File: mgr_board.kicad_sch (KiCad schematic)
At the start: 48 parts, among them IC1 MCP48CVB08-20E_ST, J1 Screw_Terminal_2_P5.00mm

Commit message: wip
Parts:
- added R49, R50, R51, R52, R53, R54, R55, R56, R57, R58, R59, R60, R61, R62: NMT, Resistor_SMD:R_0402_1005Metric, symbol PCM_SL_Resistors:Resistor
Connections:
- net +3V3: now also R1.2; no longer TH1.1
- net ADC0_CS: now also R55.2; no longer A1.2 (GP1)
- net ADC1_CS: now also R54.2; no longer A1.7 (GP5)
- net ADC2_CS: now also R57.2; no longer A1.12 (GP9)
- net ADC_NTC: now also R1.1, TH1.1; no longer R1.2, TH1.2
- net ADIM_2: now also IC1.13 (VOUT5); no longer IC1.7 (VOUT4)
- net ADIM_3: now also IC1.7 (VOUT4); no longer IC1.13 (VOUT5)
- net ADIM_4: now also IC1.14 (VOUT3); no longer IC1.6 (VOUT2)
- net ADIM_5: now also IC1.6 (VOUT2); no longer IC1.14 (VOUT3)
- net DAC_CS: now also R51.2; no longer A1.17 (GP13)
- net GND: now also TH1.2; no longer R1.1
- net SD_CS: now also R56.1; no longer A1.22 (GP17)
- net SPI0_MISO: now also R58.1, R59.1, R60.1; no longer ADC1.26 (DOUT/~{DRDY}), ADC2.26 (DOUT/~{DRDY}), ADC3.26 (DOUT/~{DRDY})
- net SPI0_MOSI: now also R52.2; no longer A1.5 (GP3)
- net SPI0_SCL: now also R53.2; no longer A1.4 (GP2)
- net SPI1_MISO: now also R61.1, R62.1; no longer IC1.17 (SDO)
- net SPI1_MOSI: now also R49.2; no longer A1.15 (GP11)
- net SPI1_SCL: now also R50.2; no longer A1.14 (GP10)
- new net: A1.5 (GP3), R52.1
- new net: ADC3.26 (DOUT/~{DRDY}), R58.2
- new net: A1.12 (GP9), R57.1
- new net: A1.14 (GP10), R50.1
- new net: A1.15 (GP11), R49.1
- new net: A1.17 (GP13), R51.1
- new net: A1.2 (GP1), R55.1
- new net: A1.22 (GP17), R56.2
- new net: A1.4 (GP2), R53.1
- new net: A1.7 (GP5), R54.1
- new net: ADC1.26 (DOUT/~{DRDY}), R60.2
- new net: ADC2.26 (DOUT/~{DRDY}), R59.2
- new net: IC1.17 (SDO), R61.2
- new net Micro_SD/SPI1_MISO: R62.2
- no-connect marks 26 -> 27
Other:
- moved on the sheet: R1, TH1

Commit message: wip
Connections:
- net +12V: now also J1.1; no longer J1.2
- net GND: now also J1.2; no longer J1.1
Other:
- moved on the sheet: J1
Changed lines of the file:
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@@
 	)
 	(junction
-		(at 201.93 26.67)
+		(at 27.94 153.67)
 		(diameter 0)
 		(color 0 0 0 0)
 	)
 	(junction
-		(at 27.94 153.67)
+		(at 201.93 26.67)
 		(diameter 0)
 		(color 0 0 0 0)
@@
 	(wire
 		(pts
+			(xy 24.13 156.21) (xy 27.94 156.21)
+		)
+		(stroke
+			(width 0)
+			(type default)
+		)
+	)
+	(wire
+		(pts
 			(xy 271.78 110.49) (xy 260.35 110.49)
 		)
@@
 	(wire
 		(pts
-			(xy 25.4 153.67) (xy 27.94 153.67)
-		)
-		(stroke
-			(width 0)
-			(type default)
-		)
-	)
-	(wire
-		(pts
 			(xy 125.73 92.71) (xy 134.62 92.71)
 		)
@@
 	(wire
 		(pts
-			(xy 27.94 156.21) (xy 25.4 156.21)
-		)
-		(stroke
-			(width 0)
-			(type default)
-		)
-	)
-	(wire
-		(pts
 			(xy 260.35 41.91) (xy 261.62 41.91)
 		)
@@
 	(wire
 		(pts
+			(xy 24.13 153.67) (xy 27.94 153.67)
+		)
+		(stroke
+			(width 0)
+			(type default)
+		)
+	)
+	(wire
+		(pts
 			(xy 260.35 31.75) (xy 280.67 31.75)
 		)
@@
 	(symbol
 		(lib_id "PCM_SL_Screw_Terminal:Screw_Terminal_2_P5.00mm")
-		(at 21.59 154.94 180)
+		(at 20.32 154.94 0)
+		(mirror y)
 		(unit 1)
 		(exclude_from_sim no)
@@
 		(dnp no)
 		(property "Reference" "J1"
-			(at 17.78 156.2101 0)
+			(at 16.51 153.6699 0)
 			(effects
 				(font
@@
 		)
 		(property "Value" "Screw_Terminal_2_P5.00mm"
-			(at 38.608 147.32 0)
+			(at 37.338 162.56 0)
 			(effects
 				(font
@@
 		)
 		(property "Footprint" "TerminalBlock:TerminalBlock_bornier-2_P5.08mm"
-			(at 20.32 148.59 0)
+			(at 19.05 161.29 0)
 			(effects
 				(font
@@
 		)
 		(property "Datasheet" ""
-			(at 21.59 154.94 0)
+			(at 20.32 154.94 0)
 			(effects
 				(font
@@
 		)
 		(property "Description" ""
-			(at 21.59 154.94 0)
+			(at 20.32 154.94 0)
 			(effects
 				(font

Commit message: finished boarD
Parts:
- C1, C3: LCSC (none) -> C19666
- C10, C11, C12, C13, C2, C4, C8, C9: LCSC (none) -> C14663
- C5, C6, C7: LCSC (none) -> C15849
- R1: LCSC (none) -> C21190
- R2, R3, R4: LCSC (none) -> C25804

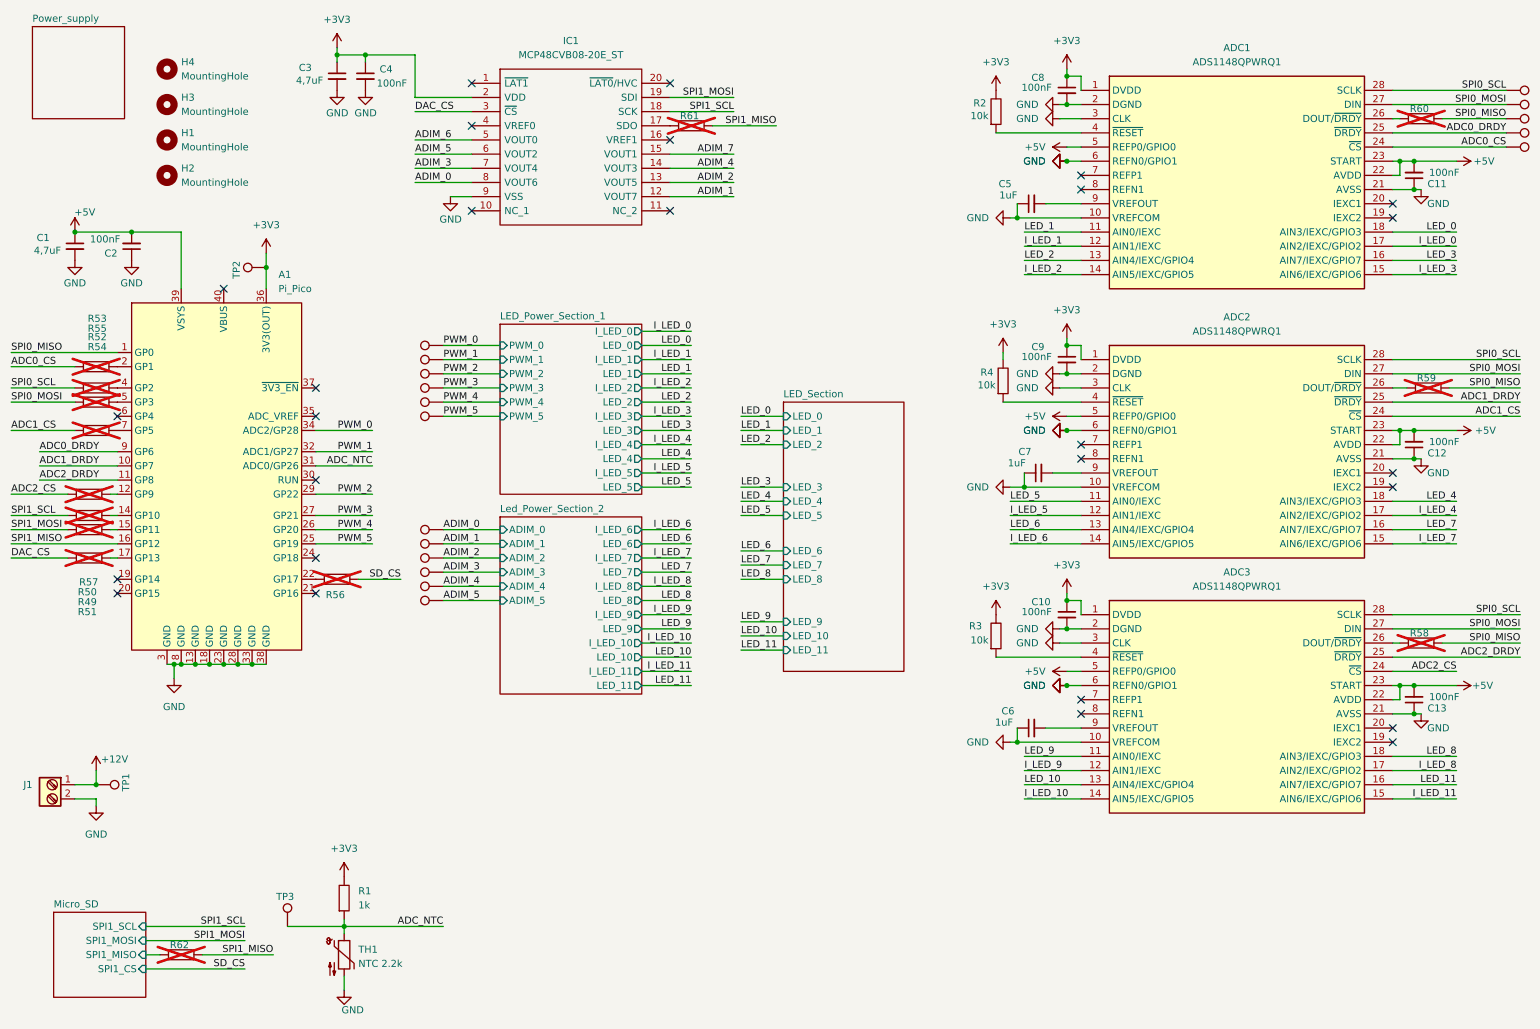
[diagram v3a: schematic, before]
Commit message: Added current sense amplifier, reduced one ADC, changed elec cap to tantals, to review
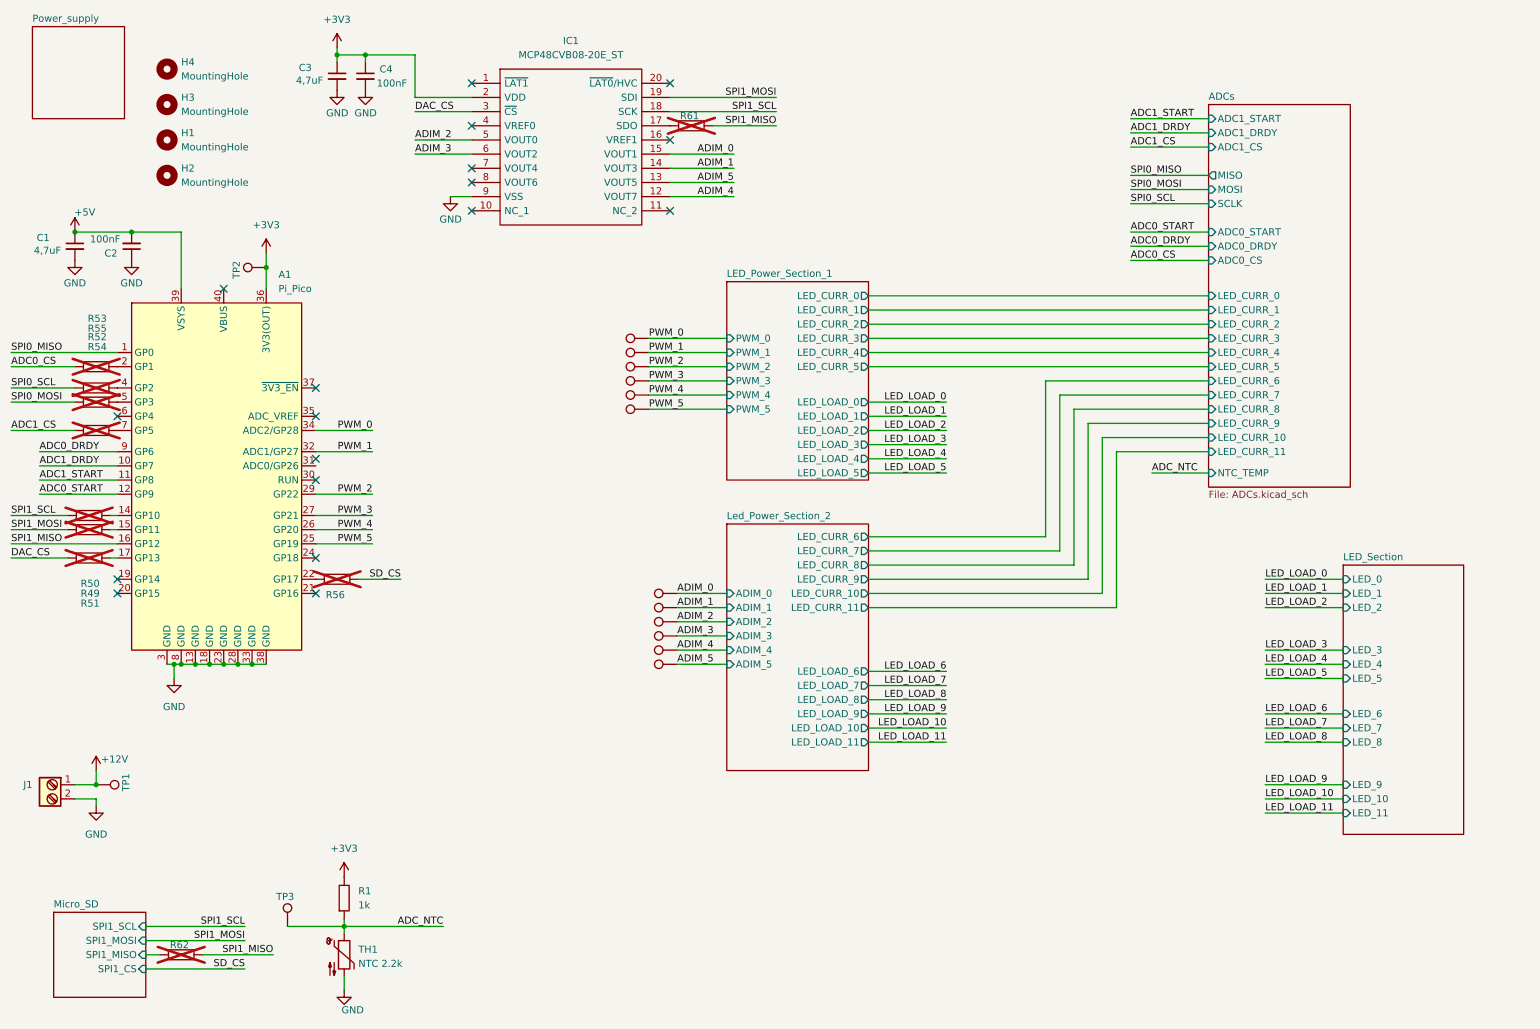
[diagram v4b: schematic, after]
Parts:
- removed ADC1, ADC2, ADC3: ADS1148QPWRQ1, Package_SO:TSSOP-28_4.4x9.7mm_P0.65mm, symbol ADS1148QPWRQ1:ADS1148QPWRQ1
- removed C10, C11, C12, C13, C8, C9: 100nF, Capacitor_SMD:C_0603_1608Metric_Pad1.08x0.95mm_HandSolder, symbol Device:C_Small
- removed C5, C6, C7: 1uF, Capacitor_SMD:C_0603_1608Metric_Pad1.08x0.95mm_HandSolder, symbol Device:C_Small
- removed R2, R3, R4: 10k, Resistor_SMD:R_0603_1608Metric_Pad0.98x0.95mm_HandSolder, symbol PCM_SL_Resistors:Resistor
- removed R57, R58, R59, R60: NMT, Resistor_SMD:R_0402_1005Metric, symbol PCM_SL_Resistors:Resistor
- removed TP16, TP17, TP18, TP19, TP20: TestPoint, TestPoint:TestPoint_Pad_D2.0mm, symbol Connector:TestPoint
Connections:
- net ADIM_6 is gone; now on net ADIM_2: IC1.5 (VOUT0)
- net ADIM_7 is gone; now on net ADIM_0: IC1.15 (VOUT1)
- net ADC_NTC: no longer A1.31 (ADC0/GP26)
- net ADIM_0: no longer IC1.8 (VOUT6)
- net ADIM_1: now also IC1.14 (VOUT3); no longer IC1.12 (VOUT7)
- net ADIM_2: no longer IC1.13 (VOUT5)
- net ADIM_3: now also IC1.6 (VOUT2); no longer IC1.7 (VOUT4)
- net ADIM_4: now also IC1.12 (VOUT7); no longer IC1.14 (VOUT3)
- net ADIM_5: now also IC1.13 (VOUT5); no longer IC1.6 (VOUT2)
- net ADC0_START: now reaches A1.12 (GP9)
- net ADC2_DRDY renamed ADC1_START
- no-connect marks 27 -> 18
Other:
- added sheet ADCs (ADCs.kicad_sch)
- sheet LED_Power_Section_1 ports: added LED_CURR_0, LED_CURR_1, LED_CURR_2, LED_CURR_3, LED_CURR_4, LED_CURR_5, LED_LOAD_0, LED_LOAD_1, LED_LOAD_2, LED_LOAD_3, LED_LOAD_4, LED_LOAD_5; removed I_LED_0, I_LED_1, I_LED_2, I_LED_3, I_LED_4, I_LED_5, LED_0, LED_1, LED_2, LED_3, LED_4, LED_5
- sheet Led_Power_Section_2 ports: added LED_CURR_10, LED_CURR_11, LED_CURR_6, LED_CURR_7, LED_CURR_8, LED_CURR_9, LED_LOAD_10, LED_LOAD_11, LED_LOAD_6, LED_LOAD_7, LED_LOAD_8, LED_LOAD_9; removed I_LED_10, I_LED_11, I_LED_6, I_LED_7, I_LED_8, I_LED_9, LED_10, LED_11, LED_6, LED_7, LED_8, LED_9

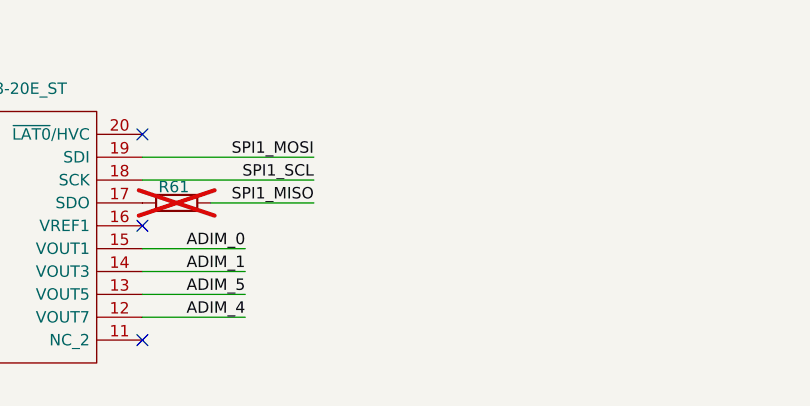
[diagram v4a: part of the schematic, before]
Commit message: Added low pass filters at current sense amp outputs and pull ups on cs pins, DRC done
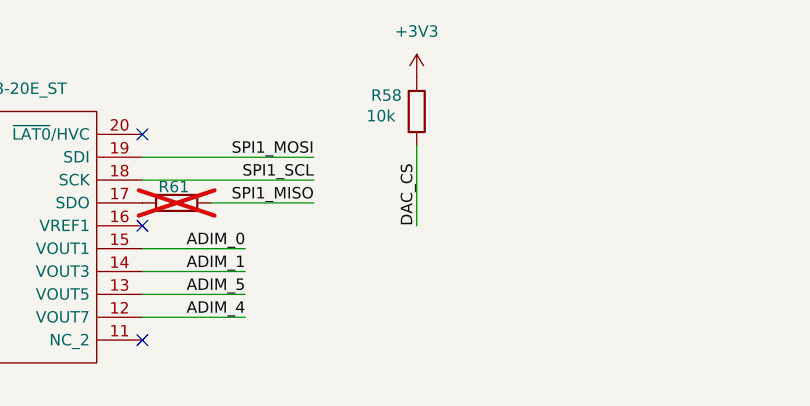
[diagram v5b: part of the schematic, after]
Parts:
- added R58: 10k, Resistor_SMD:R_0603_1608Metric_Pad0.98x0.95mm_HandSolder, symbol PCM_SL_Resistors:Resistor
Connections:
- net +3V3: now also R58.2
- net DAC_CS: now also R58.1
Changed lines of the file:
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@@
+	(wire
+		(pts
+			(xy 161.29 38.1) (xy 161.29 29.21)
+		)
+		(stroke
+			(width 0)
+			(type default)
+		)
+	)
 	(wire
 		(pts
@@
 			)
 			(justify right bottom)
+		)
+	)
+	(label "DAC_CS"
+		(at 161.29 38.1 90)
+		(effects
+			(font
+				(size 1.27 1.27)
+			)
+			(justify left bottom)
 		)
 	)
@@
 	(symbol
 		(lib_id "PCM_SL_Resistors:Resistor")
+		(at 161.29 25.4 90)
+		(unit 1)
+		(exclude_from_sim no)
+		(in_bom yes)
+		(on_board yes)
+		(dnp no)
+		(property "Reference" "R58"
+			(at 156.21 23.622 90)
+			(effects
+				(font
+					(size 1.27 1.27)
+				)
+				(justify right)
+			)
+		)
+		(property "Value" "10k"
+			(at 155.702 25.908 90)
+			(effects
+				(font
+					(size 1.27 1.27)
+				)
+				(justify right)
+			)
+		)
+		(property "Footprint" "Resistor_SMD:R_0603_1608Metric_Pad0.98x0.95mm_HandSolder"
+			(at 165.608 24.511 0)
+			(effects
+				(font
+					(size 1.27 1.27)
+				)
+				(hide yes)
+			)
+		)
+		(property "Datasheet" ""
+			(at 161.29 24.892 0)
+			(effects
+				(font
+					(size 1.27 1.27)
+				)
+				(hide yes)
+			)
+		)
+		(property "Description" "1/4W Resistor"
+			(at 161.29 25.4 0)
+			(effects
+				(font
+					(size 1.27 1.27)
+				)
+				(hide yes)
+			)
+		)
+		(property "LCSC" "C25804"
+			(at 161.29 25.4 0)
+			(effects
+				(font
+					(size 1.27 1.27)
+				)
+				(hide yes)
+			)
+		)
+		(pin "2"
+		)
+		(pin "1"
+		)
+		(instances
+			(project "mgr_board"
+				(path "/14d3b6cb-e4ae-41db-89eb-e86b07bc47b0"
+					(reference "R58")
+					(unit 1)
+				)
+			)
+		)
+	)
+	(symbol
+		(lib_id "PCM_SL_Resistors:Resistor")
 		(at 26.67 107.95 180)
 		(unit 1)
@@
 					(unit 1)
 				)
+			)
+		)
+	)
+	(symbol
+		(lib_id "power:+3V3")
+		(at 161.29 21.59 0)
+		(unit 1)
+		(exclude_from_sim no)
+		(in_bom yes)
+		(on_board yes)
+		(dnp no)
+		(fields_autoplaced yes)
+		(property "Reference" "#PWR0266"
+			(at 161.29 25.4 0)
+			(effects
+				(font
+					(size 1.27 1.27)
+				)
+				(hide yes)
+			)
+		)
+		(property "Value" "+3V3"
+			(at 161.29 16.51 0)
+			(effects
+				(font
+					(size 1.27 1.27)
+				)
+			)
+		)
+		(property "Footprint" ""
+			(at 161.29 21.59 0)
+			(effects
+				(font
+					(size 1.27 1.27)
+				)
+				(hide yes)
+			)
+		)
+		(property "Datasheet" ""
+			(at 161.29 21.59 0)
+			(effects
+				(font
+					(size 1.27 1.27)
+				)
+				(hide yes)
+			)
+		)
+		(property "Description" "Power symbol creates a global label with name \"+3V3\""
+			(at 161.29 21.59 0)
+			(effects
+				(font
+					(size 1.27 1.27)
+				)
+				(hide yes)
+			)
+		)
+		(pin "1"
+		)
+		(instances
+			(project "mgr_board"
+				(path "/14d3b6cb-e4ae-41db-89eb-e86b07bc47b0"
+					(reference "#PWR0266")
+					(unit 1)
+				)
